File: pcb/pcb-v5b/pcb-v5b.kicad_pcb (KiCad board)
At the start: 2 copper layers, 49.5 x 49.5 mm, 53 parts, among them J1 Conn_01x04, J2 Conn_01x04, J3 Conn_01x05, J4 Conn_01x05, J5 Conn_01x05, J6 Conn_01x06, Q1 2N7002, SW1 clear, SW2 +, SW3 -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

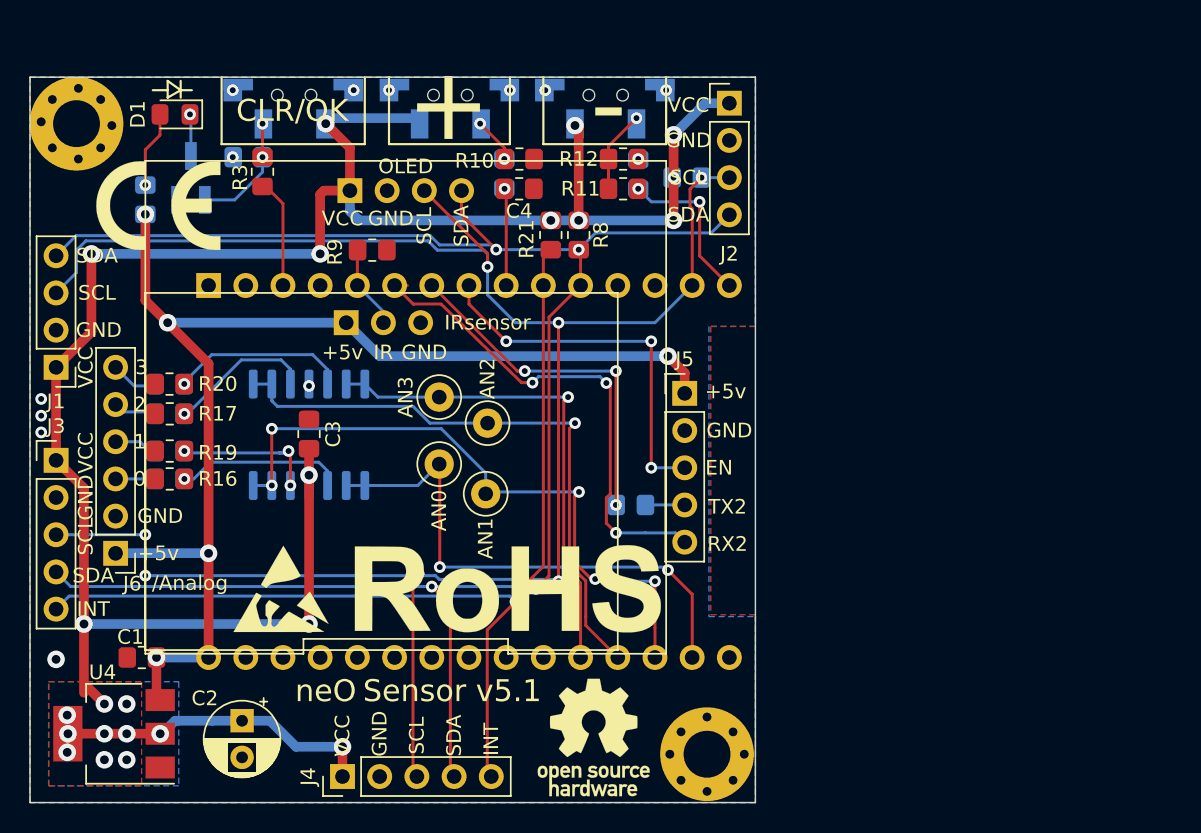
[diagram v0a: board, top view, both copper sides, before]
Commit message: updated neOSensor V5B schematic
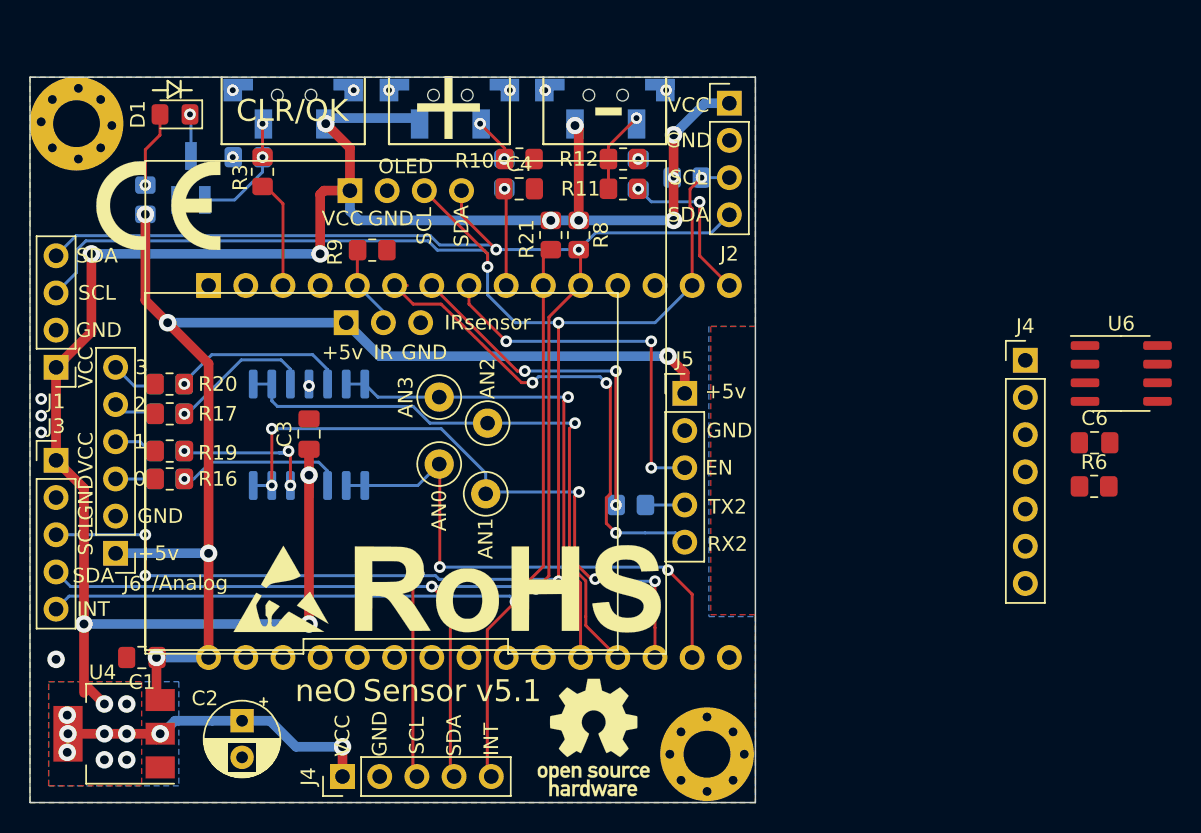
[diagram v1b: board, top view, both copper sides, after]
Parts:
- added C6: 100n, Capacitor_SMD:C_0805_2012Metric_Pad1.18x1.45mm_HandSolder, F.Cu at (98.1, 50.4)
- added J4: Conn_01x07, Connector_PinHeader_2.54mm:PinHeader_1x07_P2.54mm_Vertical, F.Cu at (93.4, 44.7)
- added R6: 470, Resistor_SMD:R_0805_2012Metric_Pad1.20x1.40mm_HandSolder, F.Cu at (98.1, 53.3)
- added U6: ATECC608A-SSHDA, Package_SO:SOIC-8_3.9x4.9mm_P1.27mm, F.Cu at (99.9, 45.6)
- C1, C3, C4, C5: footprint Resistor_SMD:R_0805_2012Metric_Pad1.20x1.40mm_HandSolder -> Capacitor_SMD:C_0805_2012Metric_Pad1.18x1.45mm_HandSolder
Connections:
- U3 pad 1: Net-(U3-Pad1) -> unconnected-(U3-3V3-Pad1)
- U3 pad 12: Net-(U3-Pad12) -> unconnected-(U3-GPIO3-Pad12)
- U3 pad 13: Net-(U3-Pad13) -> unconnected-(U3-GPIO1-Pad13)
- U3 pad 21: Net-(U3-Pad21) -> unconnected-(U3-GPIO32-Pad21)
- U3 pad 22: Net-(U3-Pad22) -> unconnected-(U3-GPIO33-Pad22)
- U3 pad 23: Net-(U3-Pad23) -> unconnected-(U3-GPIO25-Pad23)
- U3 pad 24: Net-(U3-Pad24) -> unconnected-(U3-GPIO26-Pad24)
- U3 pad 25: Net-(U3-Pad25) -> unconnected-(U3-GPIO27-Pad25)
- U3 pad 26: Net-(U3-Pad26) -> unconnected-(U3-GPIO14-Pad26)
- U3 pad 27: Net-(U3-Pad27) -> unconnected-(U3-GPIO12-Pad27)
- U3 pad 28: Net-(U3-Pad28) -> unconnected-(U3-GPIO13-Pad28)
- U3 pad 4: Net-(U3-Pad4) -> unconnected-(U3-GPIO2-Pad4)
- U3 pad 5: /IR -> Net-(U3-GPIO4)
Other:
- net class Default removed
- net class power removed
